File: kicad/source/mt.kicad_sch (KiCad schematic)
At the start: 127 parts, among them IC1 MCP73831T-2ACI_OT, IC10 SN74HC148NSR, IC11 SN74HC148NSR, IC2 BQ29728DSER, IC3 TLV74333PDBVR, IC4 TLV9152IDR, IC5 MSPM0G3507SPMR, IC6 IS62WV1288BLL-55QLI, IC7 DAC082S085CIMMX_NOPB, IC8 SN74HC148NSR, IC9 SN74HC148NSR, J1 694106301002, J2 SJ1-3524N, J3 Conn_01x05_Pin, J4 Conn_01x09_Pin, Q1 CSD16406Q3, Q2 CSD16406Q3, U1 1043

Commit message: added input OVP, screen config jumpers
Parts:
- added D2: 5.6, Diode_SMD:D_SOD-123, symbol Device:D_Zener
- added J2: 3557-2, 3557-2:3557-2, symbol 3557-2:3557-2
- added J6, J7, J8: Conn_01x03_Pin, Connector_PinHeader_2.54mm:PinHeader_1x03_P2.54mm_Vertical, symbol Connector:Conn_01x03_Pin
- renumbered J2 to J3, J3 to J4, J4 to J5
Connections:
- net GND: now also D2.2 (A), J6.1 (Pin_1), J7.1 (Pin_1), J8.1 (Pin_1)
- net VDD: now also J6.3 (Pin_3), J7.3 (Pin_3), J8.3 (Pin_3)
- net at C2.1, D1.2 (A), IC1.4 (VDD): now also D2.1 (K), J2.2, J2.4; no longer J1.1 (POWER)
- net at J5.7 (Pin_7): now also J6.2 (Pin_2)
- net at J5.8 (Pin_8): now also J7.2 (Pin_2)
- net at J5.9 (Pin_9): now also J8.2 (Pin_2)
- new net: J1.1 (POWER), J2.1, J2.3
- no-connect marks 30 -> 27
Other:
- moved on the sheet: C4, C5, IC3, R5, R6, S1

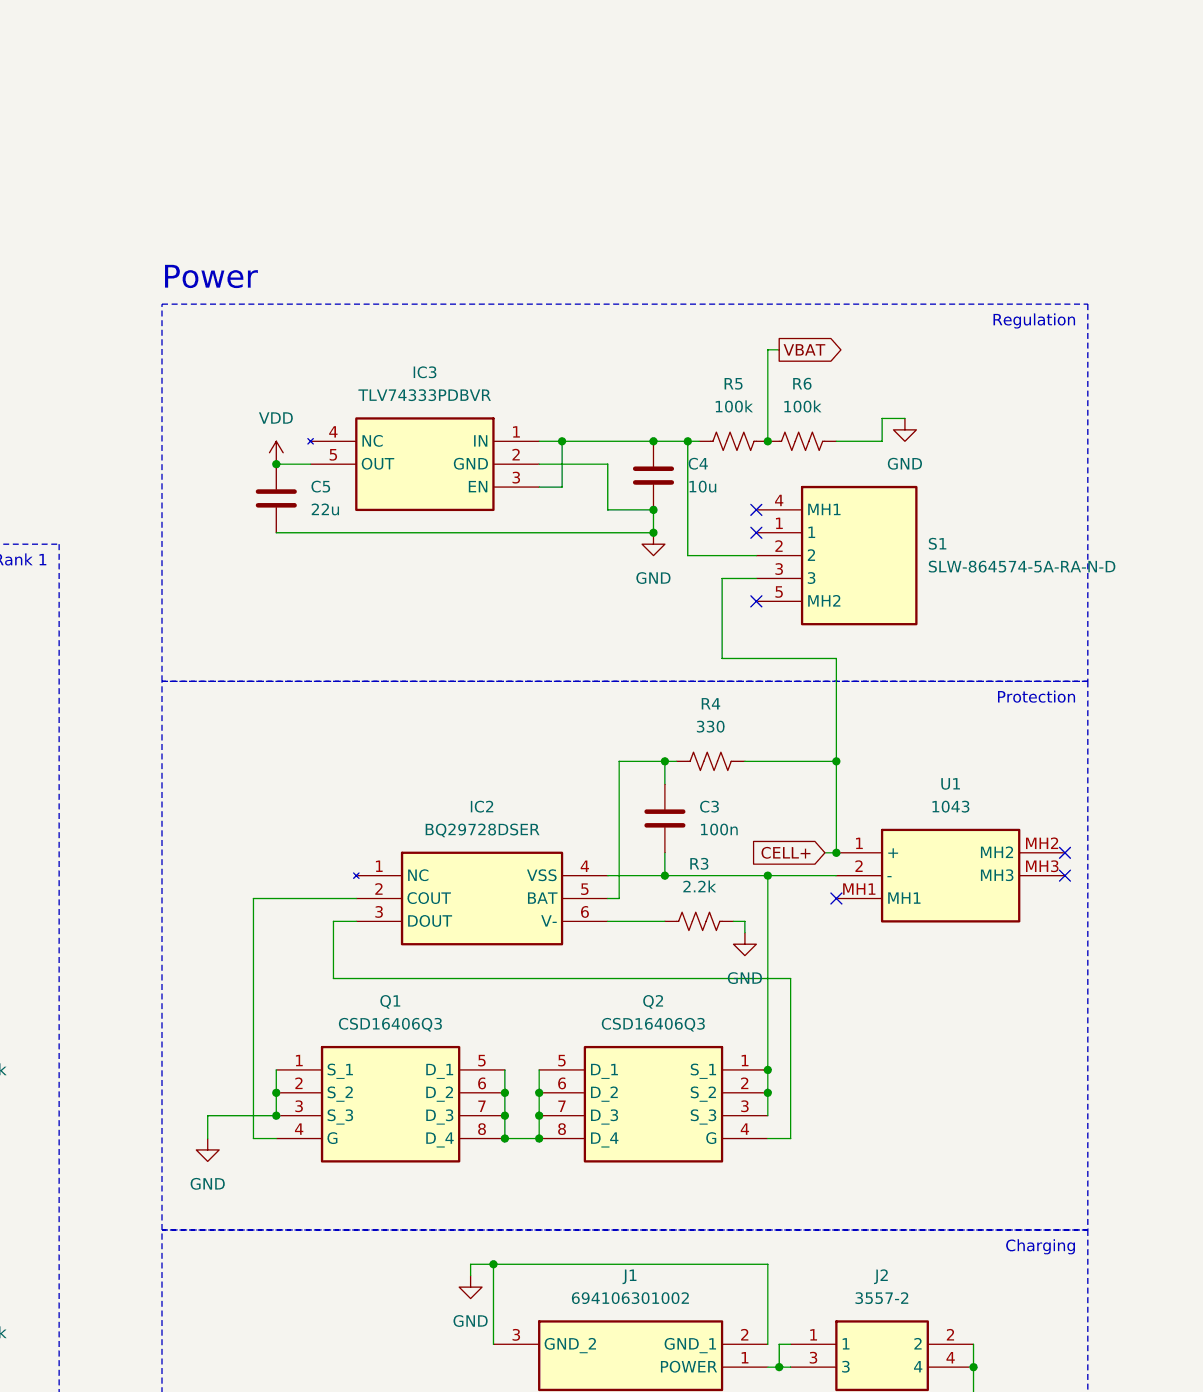
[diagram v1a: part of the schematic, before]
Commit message: completed power electronics routing, fixed battery holder model
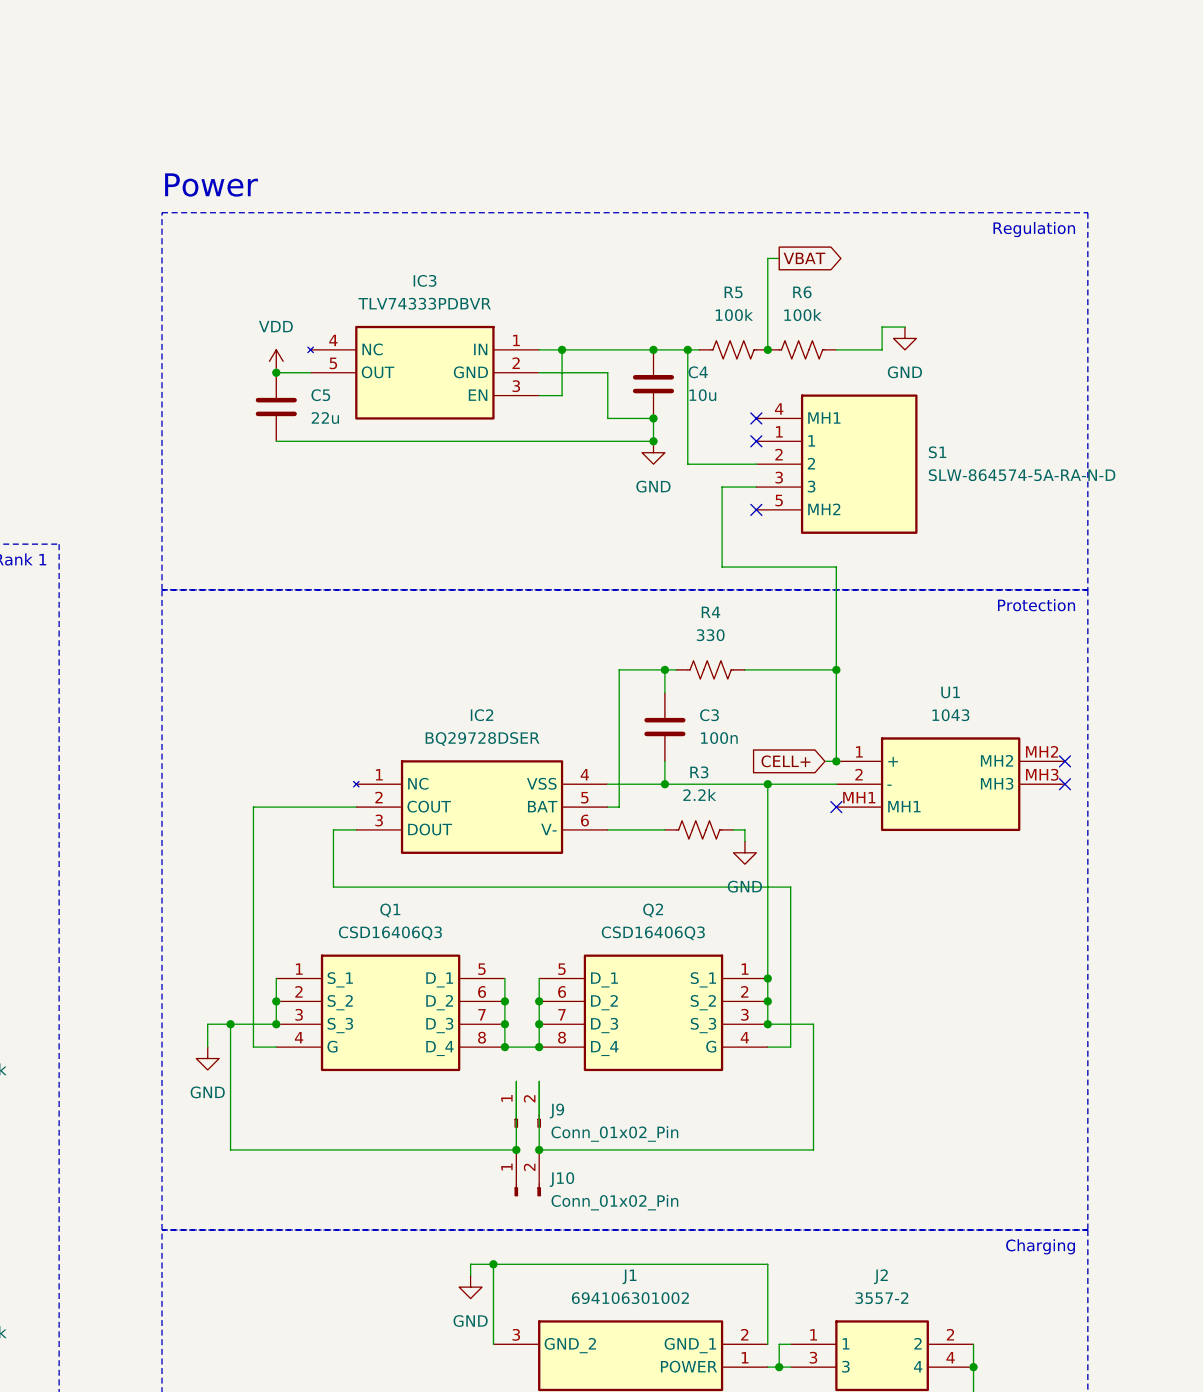
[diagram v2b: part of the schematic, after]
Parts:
- added J10, J9: Conn_01x02_Pin, Connector_PinHeader_2.54mm:PinHeader_1x02_P2.54mm_Vertical, symbol Connector:Conn_01x02_Pin
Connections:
- net GND: now also J10.1 (Pin_1), J9.1 (Pin_1)
- net at C3.2, IC2.4 (VSS), Q2.1 (S_1)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: now also J10.2 (Pin_2), J9.2 (Pin_2)
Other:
- moved on the sheet: C3, C4, C5, IC2, IC3, Q1, Q2, R3, R4, R5, R6, S1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

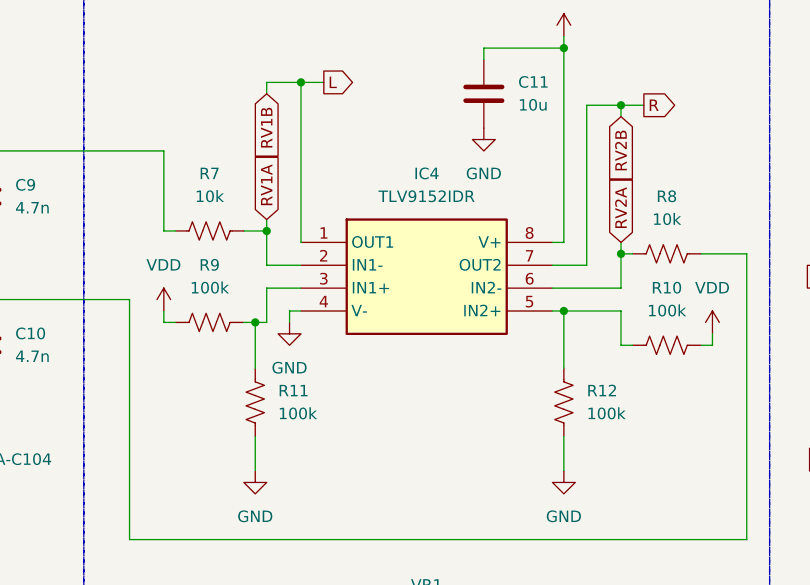
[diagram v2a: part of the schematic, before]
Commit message: completed analog electronics routing
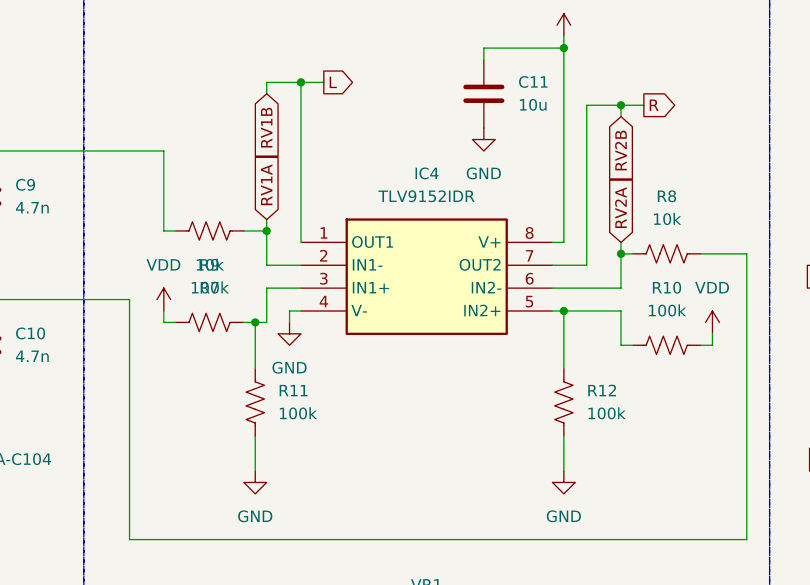
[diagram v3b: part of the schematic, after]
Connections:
- net GND: now also R12.1; no longer R12.2
- net RV1A: now also R7.2; no longer R7.1
- net at IC4.5 (IN2+), R10.1: now also R12.2; no longer R12.1
- net at C9.1, VR2.A2: now also R7.1; no longer R7.2
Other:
- moved on the sheet: R12, R7
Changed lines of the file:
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@@
 	)
 	(junction
+		(at 280.67 60.96)
+		(diameter 0)
+		(color 0 0 0 0)
+	)
+	(junction
 		(at 217.17 236.22)
 		(diameter 0)
@@
 	)
 	(junction
+		(at 313.69 69.85)
+		(diameter 0)
+		(color 0 0 0 0)
+	)
+	(junction
 		(at 110.49 45.72)
 		(diameter 0)
@@
 	)
 	(junction
-		(at 313.69 69.85)
-		(diameter 0)
-		(color 0 0 0 0)
-	)
-	(junction
 		(at 405.13 204.47)
 		(diameter 0)
@@
 	)
 	(junction
-		(at 280.67 60.96)
-		(diameter 0)
-		(color 0 0 0 0)
-	)
-	(junction
 		(at 273.05 204.47)
 		(diameter 0)
@@
 	(wire
 		(pts
-			(xy 384.81 337.82) (xy 384.81 320.04)
+			(xy 280.67 60.96) (xy 280.67 64.77)
 		)
 		(stroke
@@
 	(wire
 		(pts
-			(xy 252.73 204.47) (xy 252.73 186.69)
+			(xy 384.81 337.82) (xy 384.81 320.04)
 		)
 		(stroke
@@
 	(wire
 		(pts
-			(xy 227.33 166.37) (xy 227.33 180.34)
+			(xy 252.73 204.47) (xy 252.73 186.69)
 		)
 		(stroke
@@
 	(wire
 		(pts
-			(xy 313.69 69.85) (xy 313.69 76.2)
+			(xy 227.33 166.37) (xy 227.33 180.34)
 		)
 		(stroke
@@
 	(wire
 		(pts
+			(xy 278.13 60.96) (xy 280.67 60.96)
+		)
+		(stroke
+			(width 0)
+			(type default)
+		)
+	)
+	(wire
+		(pts
 			(xy 534.67 251.46) (xy 524.51 251.46)
 		)
@@
 	(wire
 		(pts
-			(xy 313.69 69.85) (xy 312.42 69.85)
-		)
-		(stroke
-			(width 0)
-			(type default)
-		)
-	)
-	(wire
-		(pts
 			(xy 356.87 233.68) (xy 377.19 233.68)
 		)
@@
 	(wire
 		(pts
+			(xy 269.24 60.96) (xy 270.51 60.96)
+		)
+		(stroke
+			(width 0)
+			(type default)
+		)
+	)
+	(wire
+		(pts
 			(xy 328.93 236.22) (xy 349.25 236.22)
 		)
@@
 	(wire
 		(pts
-			(xy 280.67 59.69) (xy 280.67 60.96)
-		)
-		(stroke
-			(width 0)
-			(type default)
-		)
-	)
-	(wire
-		(pts
 			(xy 412.75 236.22) (xy 433.07 236.22)
 		)
@@
 	(wire
 		(pts
+			(xy 313.69 69.85) (xy 320.04 69.85)
+		)
+		(stroke
+			(width 0)
+			(type default)
+		)
+	)
+	(wire
+		(pts
 			(xy 81.28 285.75) (xy 125.73 285.75)
 		)
@@
 	(wire
 		(pts
-			(xy 280.67 60.96) (xy 280.67 64.77)
+			(xy 280.67 59.69) (xy 280.67 60.96)
 		)
 		(stroke
@@
 	(wire
 		(pts
+			(xy 313.69 83.82) (xy 313.69 87.63)
+		)
+		(stroke
+			(width 0)
+			(type default)
+		)
+	)
+	(wire
+		(pts
 			(xy 328.93 337.82) (xy 328.93 322.58)
 		)
@@
 	(wire
 		(pts
-			(xy 320.04 69.85) (xy 313.69 69.85)
-		)
-		(stroke
-			(width 0)
-			(type default)
-		)
-	)
-	(wire
-		(pts
-			(xy 278.13 60.96) (xy 280.67 60.96)
+			(xy 312.42 69.85) (xy 313.69 69.85)
 		)
 		(stroke
@@
 	(wire
 		(pts
-			(xy 313.69 83.82) (xy 313.69 87.63)
-		)
-		(stroke
-			(width 0)
-			(type default)
-		)
-	)
-	(wire
-		(pts
 			(xy 356.87 233.68) (xy 356.87 217.17)
 		)
@@
 	(wire
 		(pts
-			(xy 269.24 60.96) (xy 270.51 60.96)
-		)
-		(stroke
-			(width 0)
-			(type default)
-		)
-	)
-	(wire
-		(pts
 			(xy 320.04 73.66) (xy 321.31 73.66)
 		)
@@
 	(wire
 		(pts
+			(xy 313.69 69.85) (xy 313.69 76.2)
+		)
+		(stroke
+			(width 0)
+			(type default)
+		)
+	)
+	(wire
+		(pts
 			(xy 224.79 337.82) (xy 245.11 337.82)
 		)
@@
 	(symbol
 		(lib_id "Device:R_US")
-		(at 274.32 60.96 270)
+		(at 274.32 60.96 90)
 		(unit 1)
 		(exclude_from_sim no)
@@
 		(dnp no)
 		(property "Reference" "R7"
-			(at 274.32 54.61 90)
+			(at 274.32 67.31 90)
 			(effects
 				(font
@@
 		)
 		(property "Value" "10k"
-			(at 274.32 57.15 90)
+			(at 274.32 64.77 90)
 			(effects
 				(font
@@
 		)
 		(property "Footprint" "Resistor_SMD:R_0402_1005Metric"
-			(at 274.066 61.976 90)
+			(at 274.574 59.944 90)
 			(effects
 				(font
@@
 	(symbol
 		(lib_id "Device:R_US")
-		(at 313.69 80.01 0)
+		(at 313.69 80.01 180)
 		(unit 1)
 		(exclude_from_sim no)
@@
 					(size 1.27 1.27)
 				)
-				(justify left)
+				(justify right)
 			)
 		)
@@
 					(size 1.27 1.27)
 				)
-				(justify left)
+				(justify right)
 			)
 		)
 		(property "Footprint" "Resistor_SMD:R_0402_1005Metric"
-			(at 314.706 80.264 90)
+			(at 312.674 79.756 90)
 			(effects
 				(font

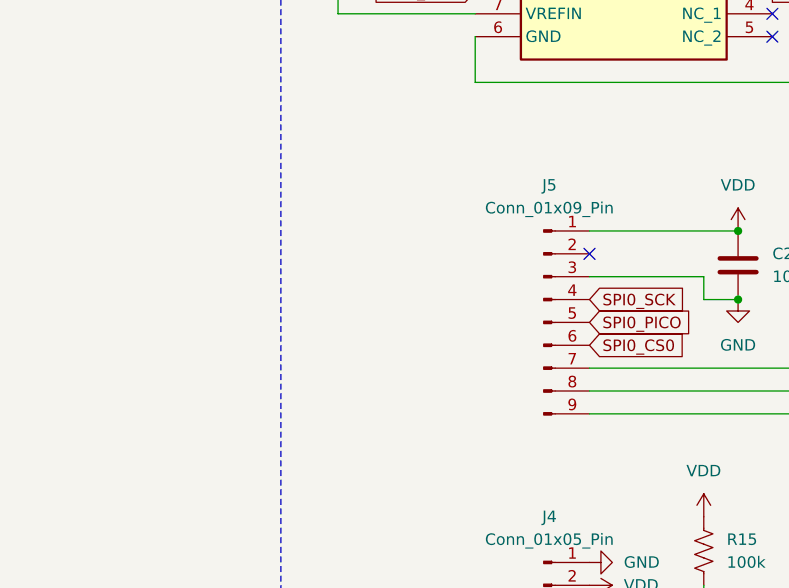
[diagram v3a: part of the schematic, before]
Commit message: completed peripherals routing, set up zone fills
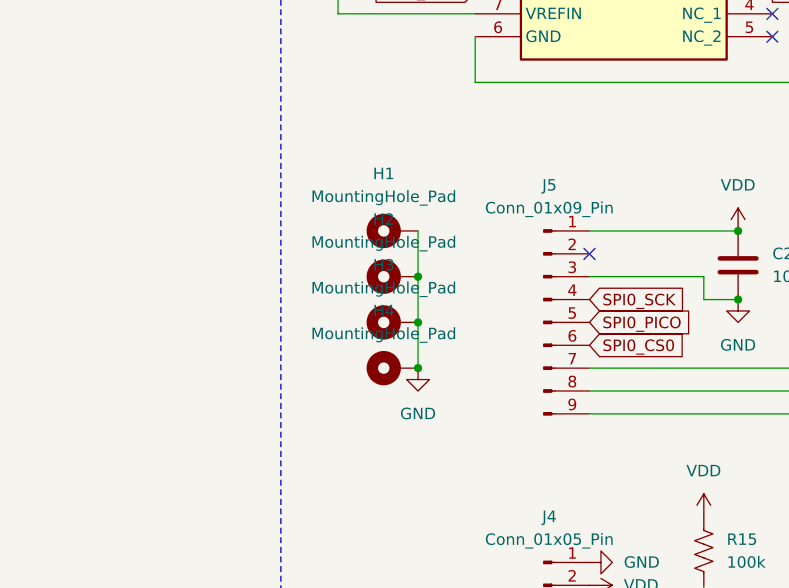
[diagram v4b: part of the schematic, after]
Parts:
- added H1, H2, H3, H4: MountingHole_Pad, MountingHole:MountingHole_3.2mm_M3_Pad_Via, symbol Mechanical:MountingHole_Pad
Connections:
- net GND: now also H1.1, H2.1, H3.1, H4.1

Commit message: converted button ranks to hierarchical schematics, prepared button layout pattern
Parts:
- removed C22, C23, C24, C25: 10u, Capacitor_SMD:C_0402_1005Metric, symbol Device:C
- removed IC10, IC11, IC8, IC9: SN74HC148NSR, SN74HC148NSR:SOIC127P780X200-16N, symbol SN74HC148NSR:SN74HC148NSR
- removed R16, R17, R18, R19, R20, R21, R22, R23, R24, R25, R26, R27, R28, R29, R30, R31, R32, R33, R34, R35, R36, R37, R38, R39, R40, R41, R42, R43, R44, R45, R46, R47: 100k, Resistor_SMD:R_0402_1005Metric, symbol Device:R_US
- removed S10, S11, S12, S13, S14, S15, S16, S17, S18, S19, S2, S20, S21, S22, S23, S24, S25, S26, S27, S28, S29, S3, S30, S31, S32, S33, S4, S5, S6, S7, S8, S9: TL6800AF160QJ, TL6800AF160QJ:TL6800AF160QJ, symbol TL6800AF160QJ:TL6800AF160QJ
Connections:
- no-connect marks 27 -> 23
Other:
- added sheet Rank 0 (rank.kicad_sch)
- added sheet Rank 1 (rank.kicad_sch)
- added sheet Rank 2 (rank.kicad_sch)
- added sheet Rank 3 (rank.kicad_sch)
- note removed: "Rank 0"
- note removed: "Rank 1"
- note removed: "Rank 2"
- note removed: "Rank 3"
- moved on the sheet: C1, C10, C11, C12, C13, C14, C15, C16, C17, C18, C19, C2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

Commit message: completed PCB fab setup
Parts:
- S34, S35: now not fitted
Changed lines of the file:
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@@
 		(in_bom yes)
 		(on_board yes)
-		(dnp no)
+		(dnp yes)
 		(fields_autoplaced yes)
 		(property "Reference" "S35"
@@
 		(in_bom yes)
 		(on_board yes)
-		(dnp no)
+		(dnp yes)
 		(fields_autoplaced yes)
 		(property "Reference" "S34"

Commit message: adjusted PCB fab setup for faster manufacturing
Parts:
- C10, C9: footprint Capacitor_SMD:C_0402_1005Metric -> Capacitor_SMD:C_0603_1608Metric_Pad1.08x0.95mm_HandSolder; now not fitted
- C12, C13, C3: footprint Capacitor_SMD:C_1206_3216Metric -> Capacitor_SMD:C_1206_3216Metric_Pad1.33x1.80mm_HandSolder; now not fitted
- IC1, IC2, IC3, IC4, IC5, IC6, IC7, Q1, Q2, S1: now not fitted
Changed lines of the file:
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@@
 		(in_bom yes)
 		(on_board yes)
-		(dnp no)
+		(dnp yes)
 		(property "Reference" "IC3"
 			(at 431.8 179.07 0)
@@
 		(in_bom yes)
 		(on_board yes)
-		(dnp no)
+		(dnp yes)
 		(fields_autoplaced yes)
 		(property "Reference" "C13"
@@
 			)
 		)
-		(property "Footprint" "Capacitor_SMD:C_1206_3216Metric"
+		(property "Footprint" "Capacitor_SMD:C_1206_3216Metric_Pad1.33x1.80mm_HandSolder"
 			(at 417.83 84.1248 0)
 			(effects
@@
 		(in_bom yes)
 		(on_board yes)
-		(dnp no)
+		(dnp yes)
 		(fields_autoplaced yes)
 		(property "Reference" "IC4"
@@
 		(in_bom yes)
 		(on_board yes)
-		(dnp no)
+		(dnp yes)
 		(fields_autoplaced yes)
 		(property "Reference" "IC7"
@@
 		(in_bom yes)
 		(on_board yes)
-		(dnp no)
+		(dnp yes)
 		(fields_autoplaced yes)
 		(property "Reference" "Q1"
@@
 		(in_bom yes)
 		(on_board yes)
-		(dnp no)
+		(dnp yes)
 		(fields_autoplaced yes)
 		(property "Reference" "IC2"
@@
 		(in_bom yes)
 		(on_board yes)
-		(dnp no)
+		(dnp yes)
 		(property "Reference" "Q2"
 			(at 457.2 248.92 0)
@@
 		(in_bom yes)
 		(on_board yes)
-		(dnp no)
+		(dnp yes)
 		(fields_autoplaced yes)
 		(property "Reference" "IC5"
@@
 		(in_bom yes)
 		(on_board yes)
-		(dnp no)
+		(dnp yes)
 		(fields_autoplaced yes)
 		(property "Reference" "C9"
@@
 			)
 		)
-		(property "Footprint" "Capacitor_SMD:C_0402_1005Metric"
+		(property "Footprint" "Capacitor_SMD:C_0603_1608Metric_Pad1.08x0.95mm_HandSolder"
 			(at 313.3852 80.01 0)
 			(effects
@@
 		(in_bom yes)
 		(on_board yes)
-		(dnp no)
+		(dnp yes)
 		(fields_autoplaced yes)
 		(property "Reference" "S1"
@@
 		(in_bom yes)
 		(on_board yes)
-		(dnp no)
+		(dnp yes)
 		(fields_autoplaced yes)
 		(property "Reference" "C12"
@@
 			)
 		)
-		(property "Footprint" "Capacitor_SMD:C_1206_3216Metric"
+		(property "Footprint" "Capacitor_SMD:C_1206_3216Metric_Pad1.33x1.80mm_HandSolder"
 			(at 434.34 104.4448 0)
 			(effects
@@
 		(in_bom yes)
 		(on_board yes)
-		(dnp no)
+		(dnp yes)
 		(fields_autoplaced yes)
 		(property "Reference" "C10"
@@
 			)
 		)
-		(property "Footprint" "Capacitor_SMD:C_0402_1005Metric"
+		(property "Footprint" "Capacitor_SMD:C_0603_1608Metric_Pad1.08x0.95mm_HandSolder"
 			(at 313.3852 96.52 0)
 			(effects
@@
 		(in_bom yes)
 		(on_board yes)
-		(dnp no)
+		(dnp yes)
 		(fields_autoplaced yes)
 		(property "Reference" "C3"
@@
 			)
 		)
-		(property "Footprint" "Capacitor_SMD:C_1206_3216Metric"
+		(property "Footprint" "Capacitor_SMD:C_1206_3216Metric_Pad1.33x1.80mm_HandSolder"
 			(at 459.4352 232.41 0)
 			(effects
@@
 		(in_bom yes)
 		(on_board yes)
-		(dnp no)
+		(dnp yes)
 		(property "Reference" "IC1"
 			(at 454.66 308.61 0)
@@
 		(in_bom yes)
 		(on_board yes)
-		(dnp no)
+		(dnp yes)
 		(fields_autoplaced yes)
 		(property "Reference" "IC6"
